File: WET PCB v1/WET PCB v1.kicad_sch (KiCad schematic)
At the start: 14 parts, among them J1 XT60, J2 XT60 or Terminal, J3 Conn_01x02_Pin, Q1 Q_NMOS_Depletion_GDS, Q2 Q_NMOS_Depletion_GDS

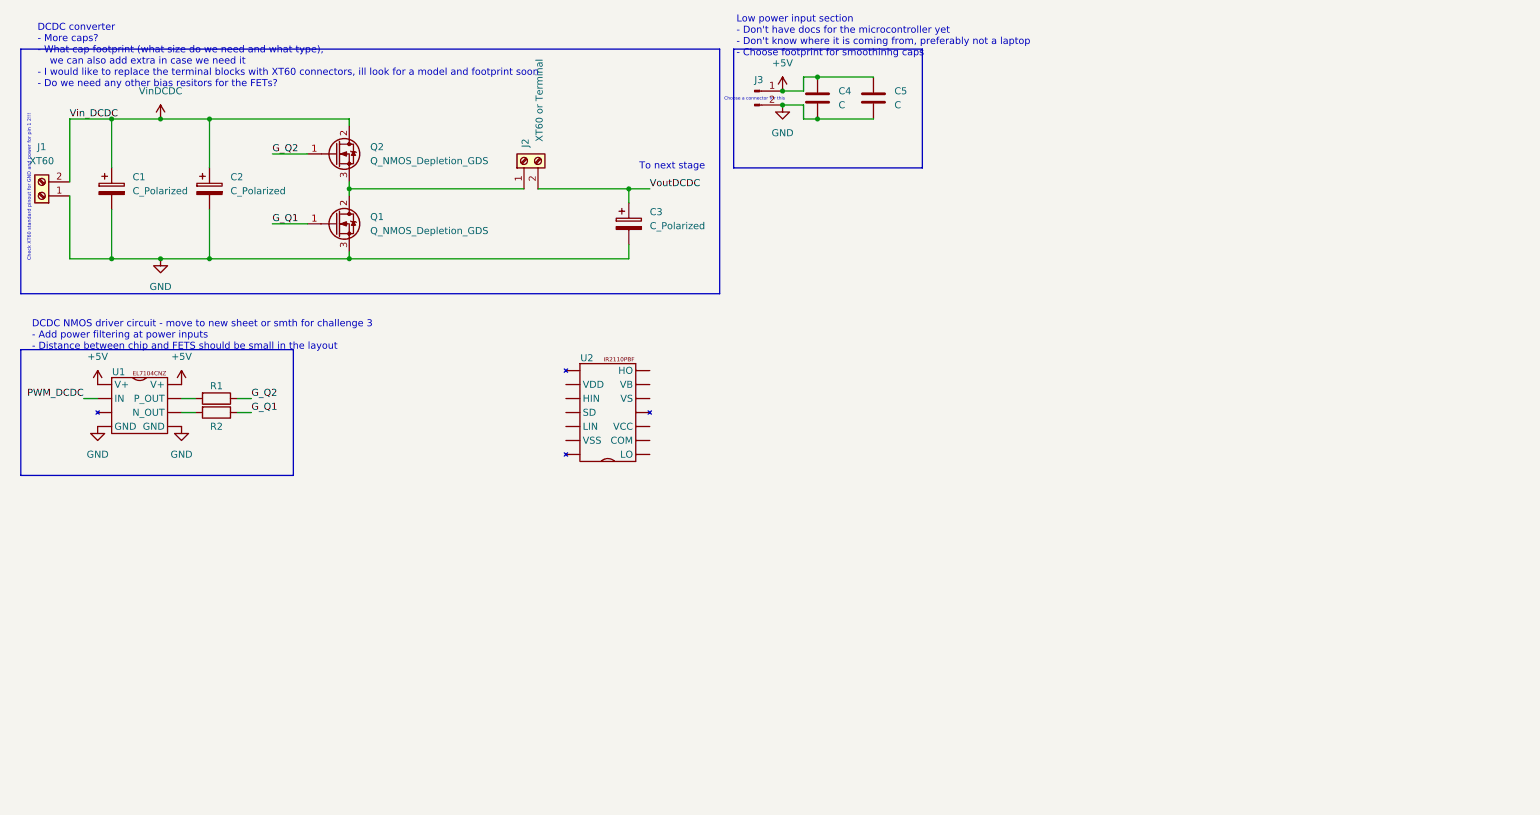
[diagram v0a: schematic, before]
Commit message: Added empty text fields for (some) missing circuits
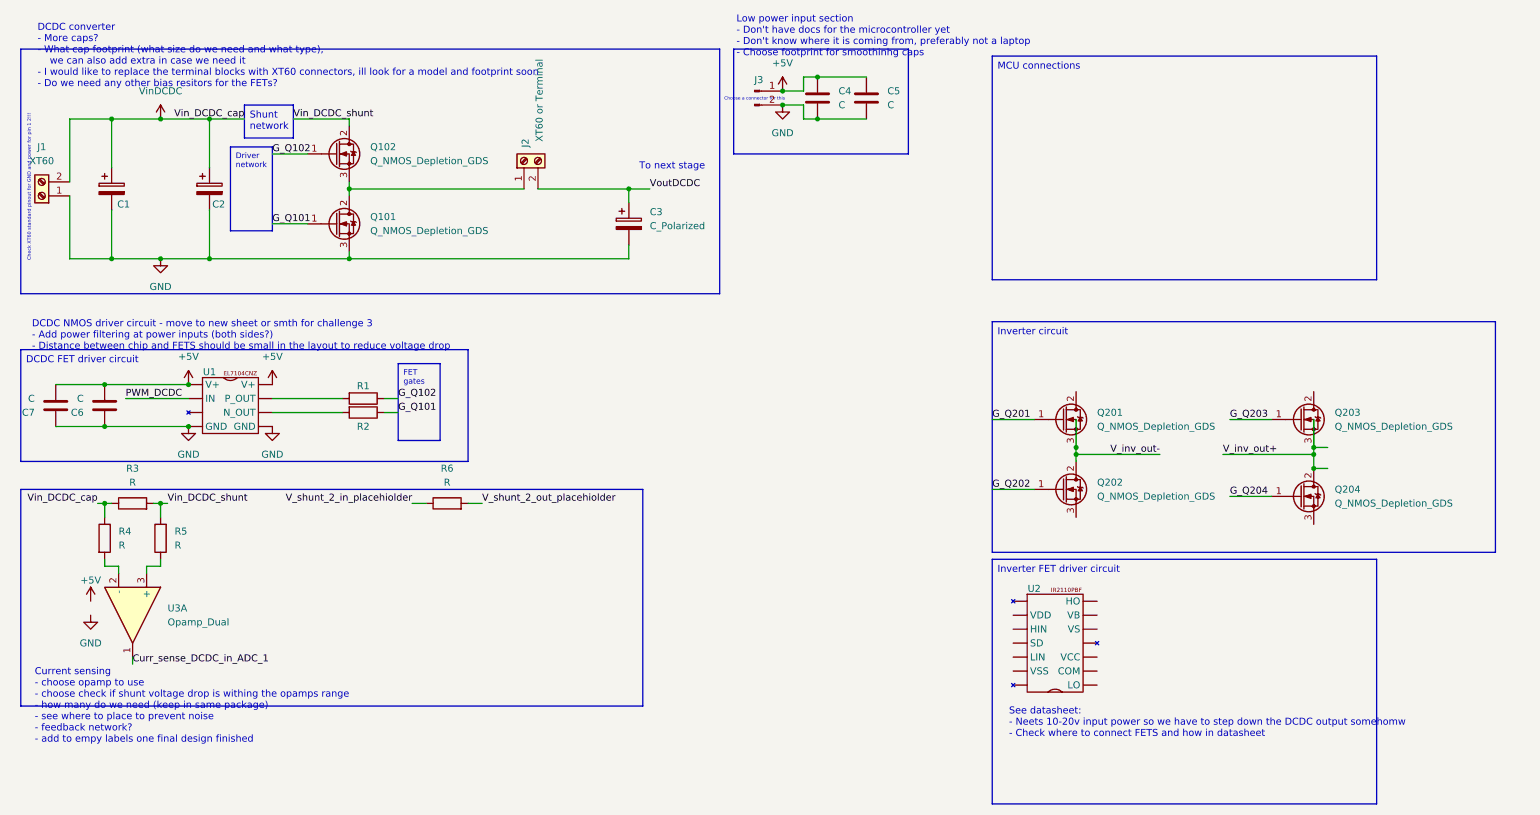
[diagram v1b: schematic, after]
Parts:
- added C6, C7: C, symbol Device:C
- added Q201, Q202, Q203, Q204: Q_NMOS_Depletion_GDS, Package_TO_SOT_THT:TO-220-3_Vertical, symbol Transistor_FET_Other:Q_NMOS_Depletion_GDS
- added R3, R4, R5, R6: R, symbol Device:R
- added U3: Opamp_Dual, symbol Device:Opamp_Dual
- renumbered Q1 to Q101, Q2 to Q102
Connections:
- net +5V: now also C6.2, C7.2
- net GND: now also C6.1, C7.1
- net VinDCDC: now also R3.1, R4.1; no longer Q102.2 (D)
- net G_Q1 renamed G_Q101
- net G_Q2 renamed G_Q102
- new net: R4.2, U3.2 (-)
- new net: R5.1, U3.3 (+)
- new net Curr_sense_DCDC_in_ADC_1: U3.1
- new net G_Q201: Q201.1 (G)
- new net G_Q202: Q202.1 (G)
- new net G_Q203: Q203.1 (G)
- new net G_Q204: Q204.1 (G)
- new net V_inv_out+: Q203.3 (S), Q204.2 (D)
- new net V_inv_out-: Q201.3 (S), Q202.2 (D)
- new net V_shunt_2_in_placehiolder: R6.1
- new net V_shunt_2_out_placehiolder: R6.2
- new net Vin_DCDC_shunt: Q102.2 (D), R3.2, R5.2
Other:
- note added: "Current sensing - choose opamp to use - choose check if shunt voltage drop is withing the opamps range - how many do we need (keep in same package) - see where to place to prevent noise - feedback network? - add to empy labels one final design finished"
- note added: "DCDC NMOS driver circuit - move to new sheet or smth for challenge 3 - Add power filtering at power inputs (both sides?) - Distance between chip and FETS should be small in the layout to reduce voltage drop"
- note added: "See datasheet: - Neets 10-20v input power so we have to step down the DCDC output somehomw - Check where to connect FETS and how in datasheet"
- note removed: "DCDC NMOS driver circuit - move to new sheet or smth for challenge 3 - Add power filtering at power inputs - Distance between chip and FETS should be small in the layout"
- moved on the sheet: C5, R1, R2, U1, U2

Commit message: Jake update friday
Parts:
- removed C1, C2: C_Polarized, symbol Device:C_Polarized
- added C1: C, symbol Device:C
- J2: value XT60 or Terminal -> XT60
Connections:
- net GND: now also C1.2; no longer Q101.3 (S)
- net VinDCDC: now also J2.2 (Pin_2), C1.1; no longer J1.2 (Pin_2)
- net Vin_DCDC_shunt: now also Q101.3 (S)
- net VoutDCDC: now also Q102.3 (S); no longer J2.2 (Pin_2)
- new net: J1.2 (Pin_2), J2.1 (Pin_1)
- now unconnected: Q101.2 (D)
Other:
- moved on the sheet: C3, Q101, Q102
